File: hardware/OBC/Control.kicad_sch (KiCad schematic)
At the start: 16 parts, among them J13 Conn_01x08_SocketMPU, J14 Conn_01x04_Socket, J15 Screw_Terminal_01x02, J16 Conn_01x02, J17 Conn_01x06_Socket, J18 Conn_01x02, J19 Conn_01x03, J20 Conn_01x02, J21 Conn_01x02, SW1 SW_SPDT, U1 25CSM04xxSN

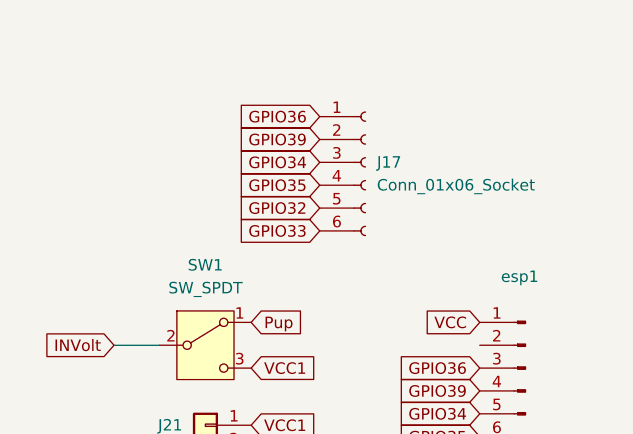
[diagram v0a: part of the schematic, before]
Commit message: Adapt Barometric Pressure Sensor in J17 connector socket
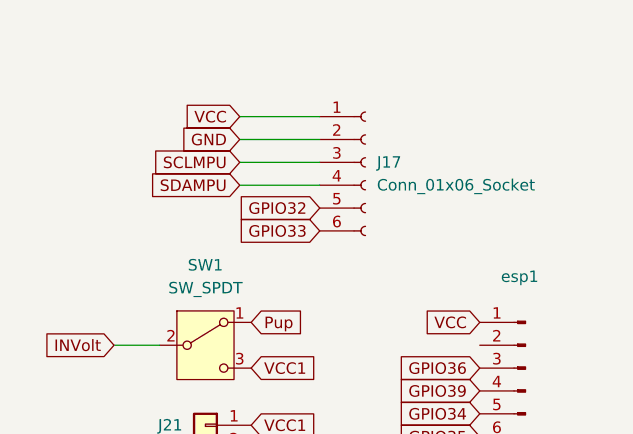
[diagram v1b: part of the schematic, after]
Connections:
- net GND: now also J17.2 (Pin_2)
- net GPIO34: no longer J17.3 (Pin_3)
- net GPIO35: no longer J17.4 (Pin_4)
- net GPIO36: no longer J17.1 (Pin_1)
- net GPIO39: no longer J17.2 (Pin_2)
- net SCLMPU: now also J17.3 (Pin_3)
- net SDAMPU: now also J17.4 (Pin_4)
- net VCC: now also J17.1 (Pin_1)
